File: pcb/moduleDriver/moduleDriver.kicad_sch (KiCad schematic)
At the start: 32 parts, among them J10 Sensor, J11 Power, J12 Power, J7 Sensor, J8 Sensor, J9 Sensor

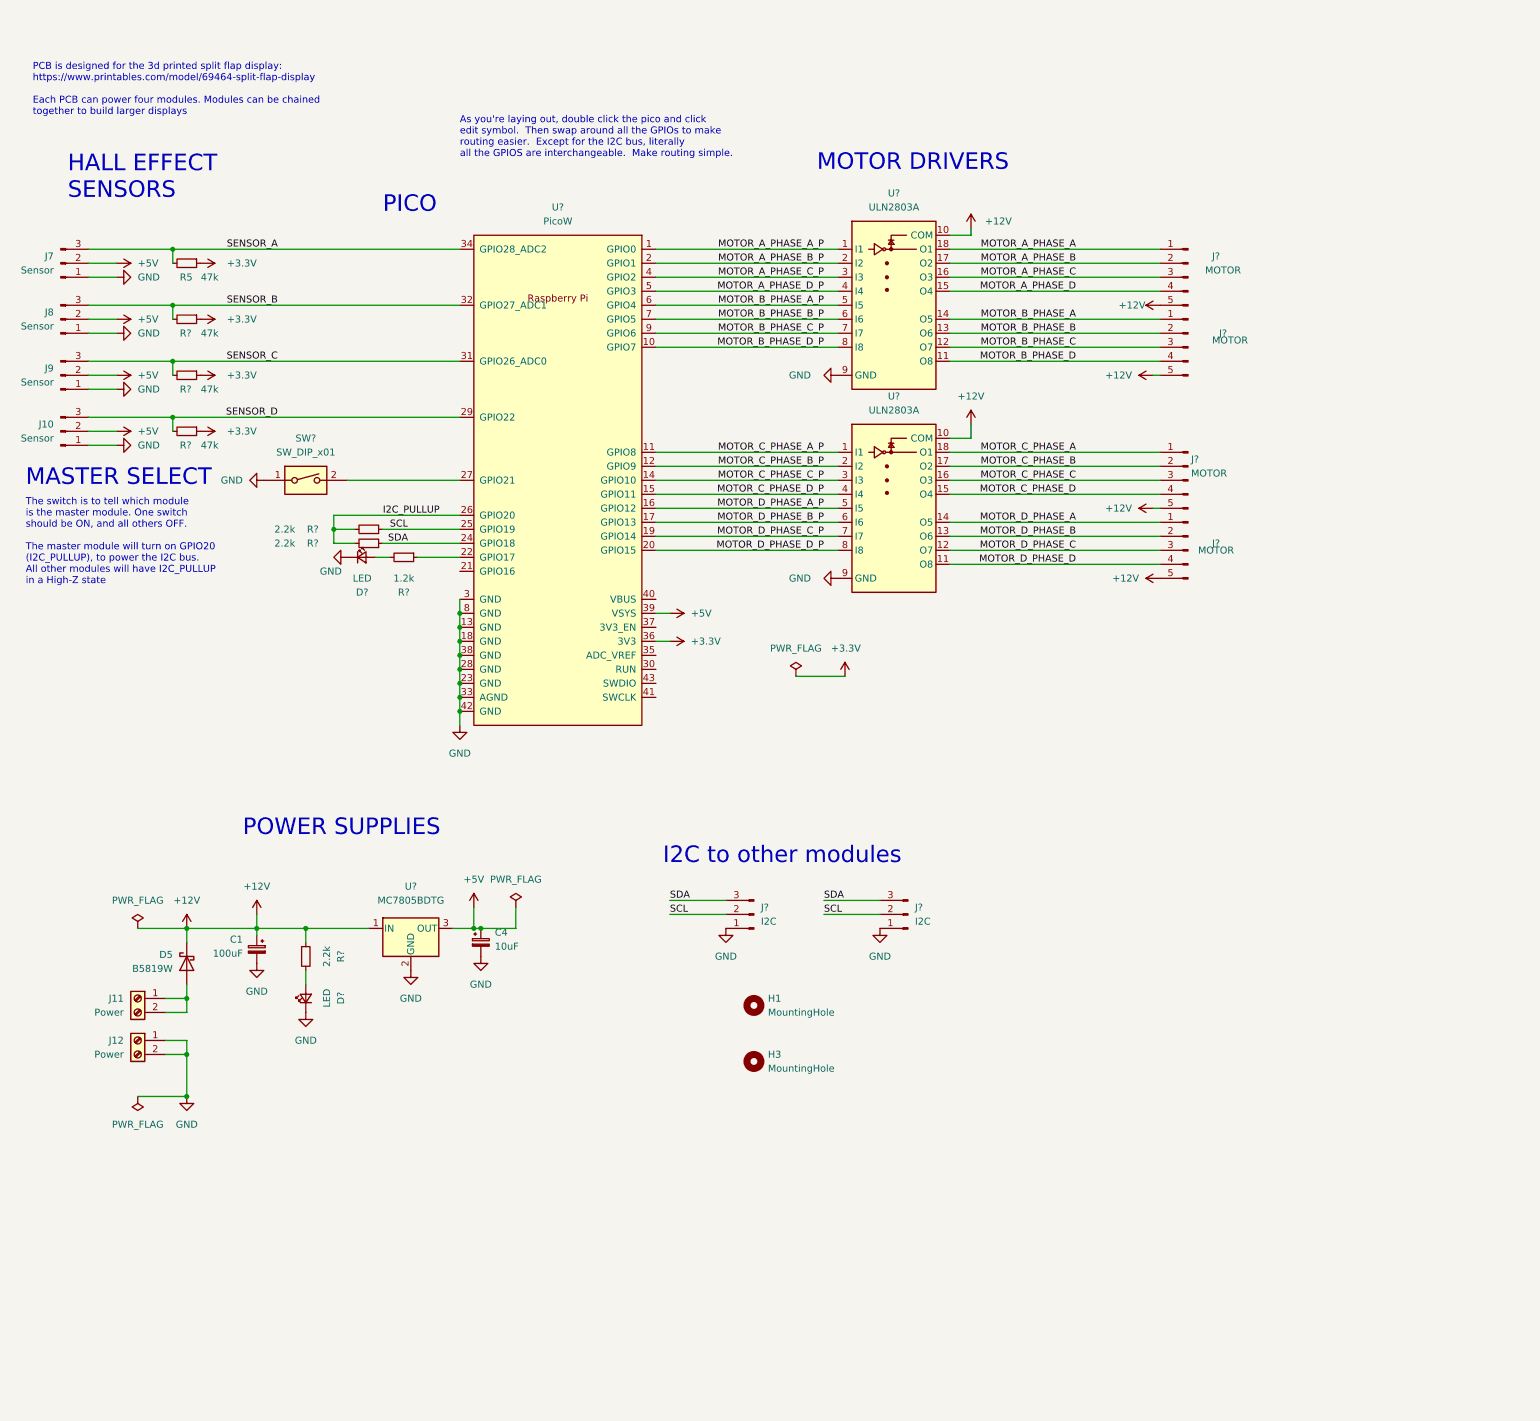
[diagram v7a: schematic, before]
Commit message: erm... added dip switches for module addressing.... and some notes.  but now there's a better way...
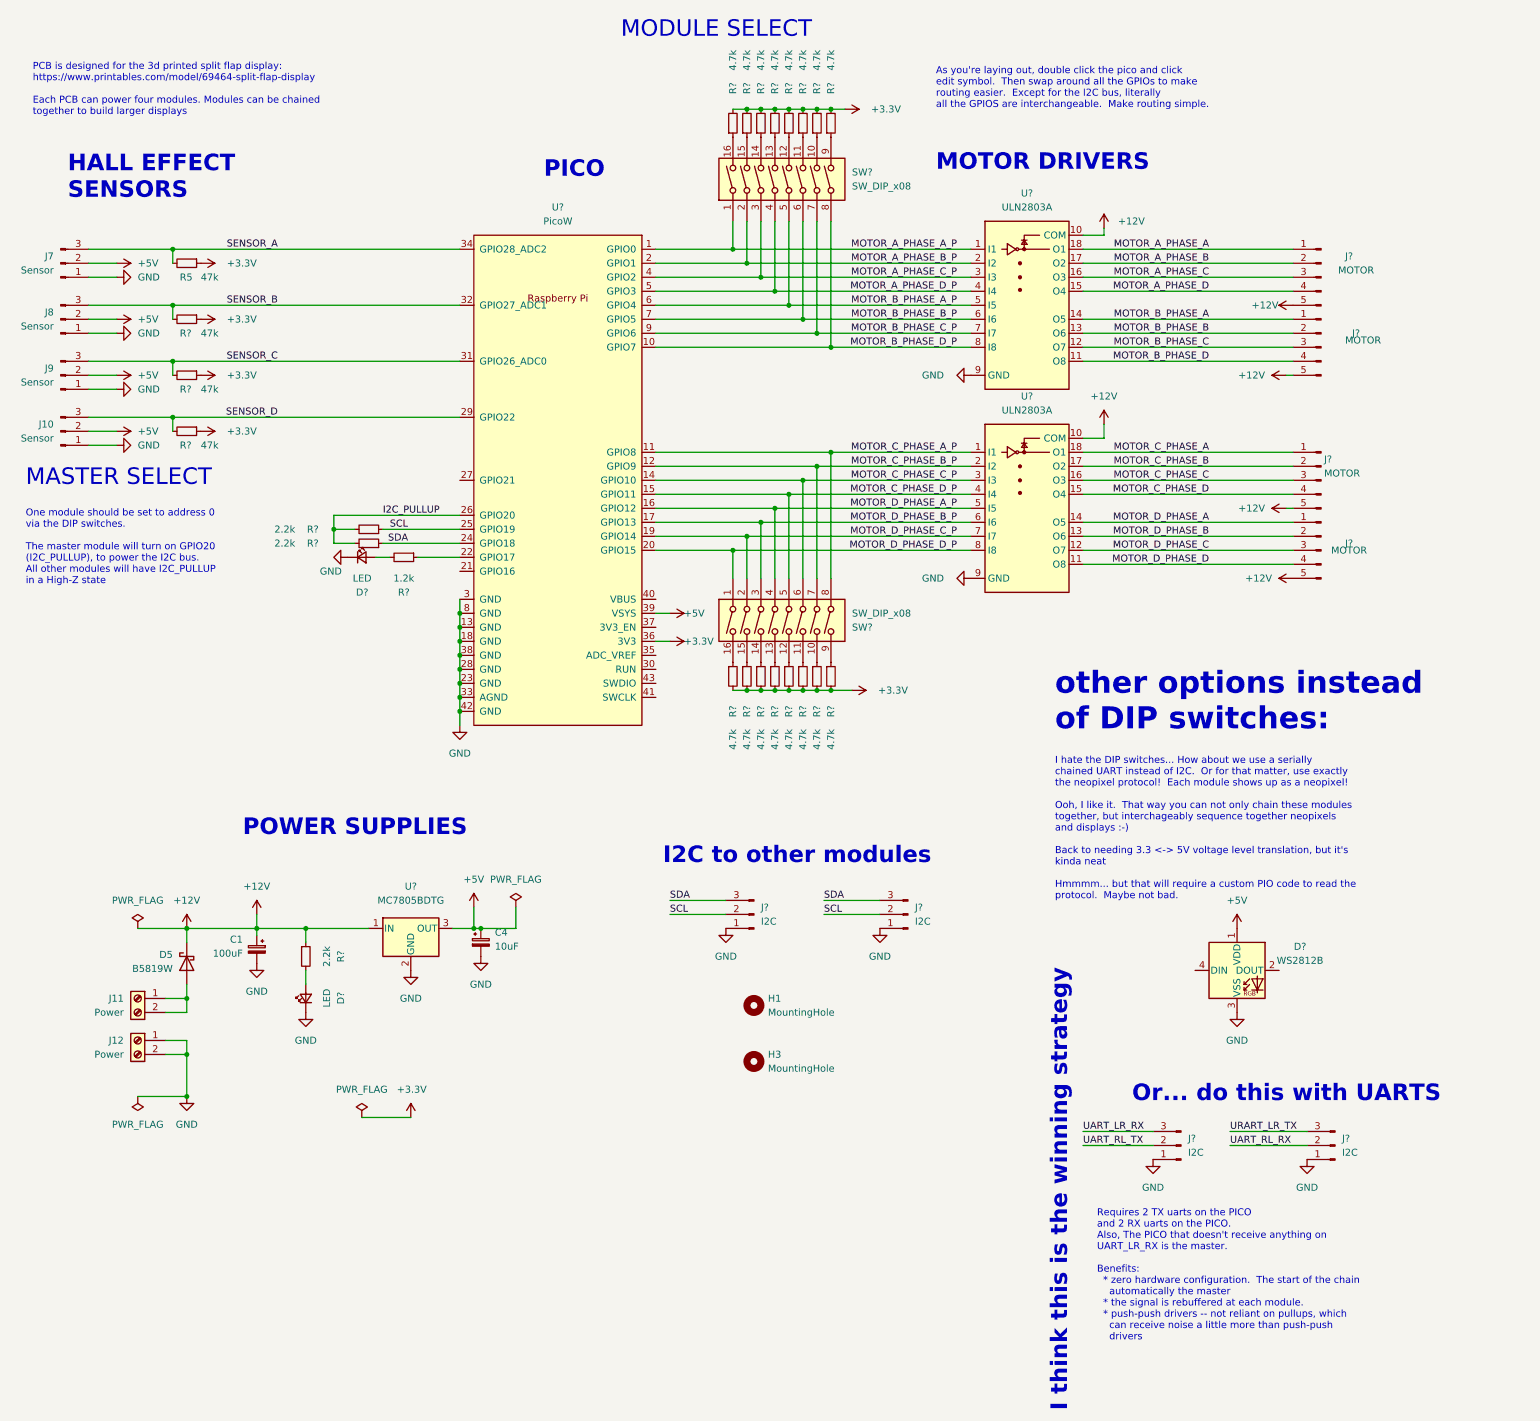
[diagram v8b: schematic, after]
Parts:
- removed SW?: SW_DIP_x01, symbol Switch:SW_DIP_x01
- added D?: WS2812B, LED_SMD:LED_WS2812B_PLCC4_5.0x5.0mm_P3.2mm, symbol LED:WS2812B
- added J? (x2): I2C, Connector_PinHeader_2.54mm:PinHeader_1x03_P2.54mm_Vertical, symbol Connector:Conn_01x03_Male
- added R? (x16): 4.7k, Resistor_SMD:R_0603_1608Metric, symbol Device:R_Small
- added SW? (x2): SW_DIP_x08, symbol Switch:SW_DIP_x08
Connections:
- net +3.3V: now also R?.2, R?.2, R?.2, R?.2, R?.2, R?.2, R?.2, R?.2, R?.2, R?.2, R?.2, R?.2, R?.2, R?.2, R?.2, R?.2
- net +5V: now also D?.1 (VDD)
- net GND: now also D?.3 (VSS), J?.1 (Pin_1), J?.1 (Pin_1)
- net MOTOR_A_PHASE_A_P: now also SW?.1
- net MOTOR_A_PHASE_B_P: now also SW?.2
- net MOTOR_A_PHASE_C_P: now also SW?.3
- net MOTOR_A_PHASE_D_P: now also SW?.4
- net MOTOR_B_PHASE_A_P: now also SW?.5
- net MOTOR_B_PHASE_B_P: now also SW?.6
- net MOTOR_B_PHASE_C_P: now also SW?.7
- net MOTOR_B_PHASE_D_P: now also SW?.8
- net MOTOR_C_PHASE_A_P: now also SW?.8
- net MOTOR_C_PHASE_B_P: now also SW?.7
- net MOTOR_C_PHASE_C_P: now also SW?.6
- net MOTOR_C_PHASE_D_P: now also SW?.5
- net MOTOR_D_PHASE_A_P: now also SW?.4
- net MOTOR_D_PHASE_B_P: now also SW?.3
- net MOTOR_D_PHASE_C_P: now also SW?.2
- net MOTOR_D_PHASE_D_P: now also SW?.1
- new net: R?.1, SW?.12 (x2)
- new net: R?.1, SW?.9 (x2)
- new net: R?.1, SW?.15 (x2)
- new net: R?.1, SW?.10 (x2)
- new net: R?.1, SW?.11 (x2)
- new net: R?.1, SW?.13 (x2)
- new net: R?.1, SW?.14 (x2)
- new net: R?.1, SW?.16 (x2)
- new net UART_LR_RX: J?.3 (Pin_3)
- new net UART_RL_RX: J?.2 (Pin_2)
- new net UART_RL_TX: J?.2 (Pin_2)
- new net URART_LR_TX: J?.3 (Pin_3)
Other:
- note added: "I hate the DIP switches... How about we use a serially chained UART instead of I2C. Or for that matter, use exactly the neopixel protocol! Each module shows up as a neopixel! Ooh, I like it. That way you can not only chain these modules together, but interchageably sequence together neopixels and displays :-) Back to needing 3.3 <-> 5V voltage level translation, but it's kinda neat Hmmmm... but t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"
- note added: "I think this is the winning strategy"
- note added: "MODULE SELECT"
- note added: "One module should be set to address 0 via the DIP switches. The master module will turn on GPIO20 (I2C_PULLUP), to power the I2C bus. All other modules will have I2C_PULLUP in a High-Z state"
- note added: "Or... do this with UARTS"
- note added: "Requires 2 TX uarts on the PICO and 2 RX uarts on the PICO. Also, The PICO that doesn't receive anything on UART_LR_RX is the master. Benefits: * zero hardware configuration. The start of the chain automatically the master * the signal is rebuffered at each module. * push-push drivers -- not reliant on pullups, which can receive noise a little more than push-push drivers"
- note added: "other options instead of DIP switches:"
- note removed: "The switch is to tell which module is the master module. One switch should be ON, and all others OFF. The master module will turn on GPIO20 (I2C_PULLUP), to power the I2C bus. All other modules will have I2C_PULLUP in a High-Z state"
- moved on the sheet: J?, U?
